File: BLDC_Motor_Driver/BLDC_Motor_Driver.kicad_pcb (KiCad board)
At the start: 4 copper layers, 95 x 95 mm, 139 parts, among them J101 Conn_01x08, J102 395221002, J103 USB4105-GF-A, J104 Conn_01x05, J105 Conn_01x05, J106 Conn_01x04, J107 395221005, J108 395221003, J109 Conn_02x12_Counter_Clockwise, J110 395221005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

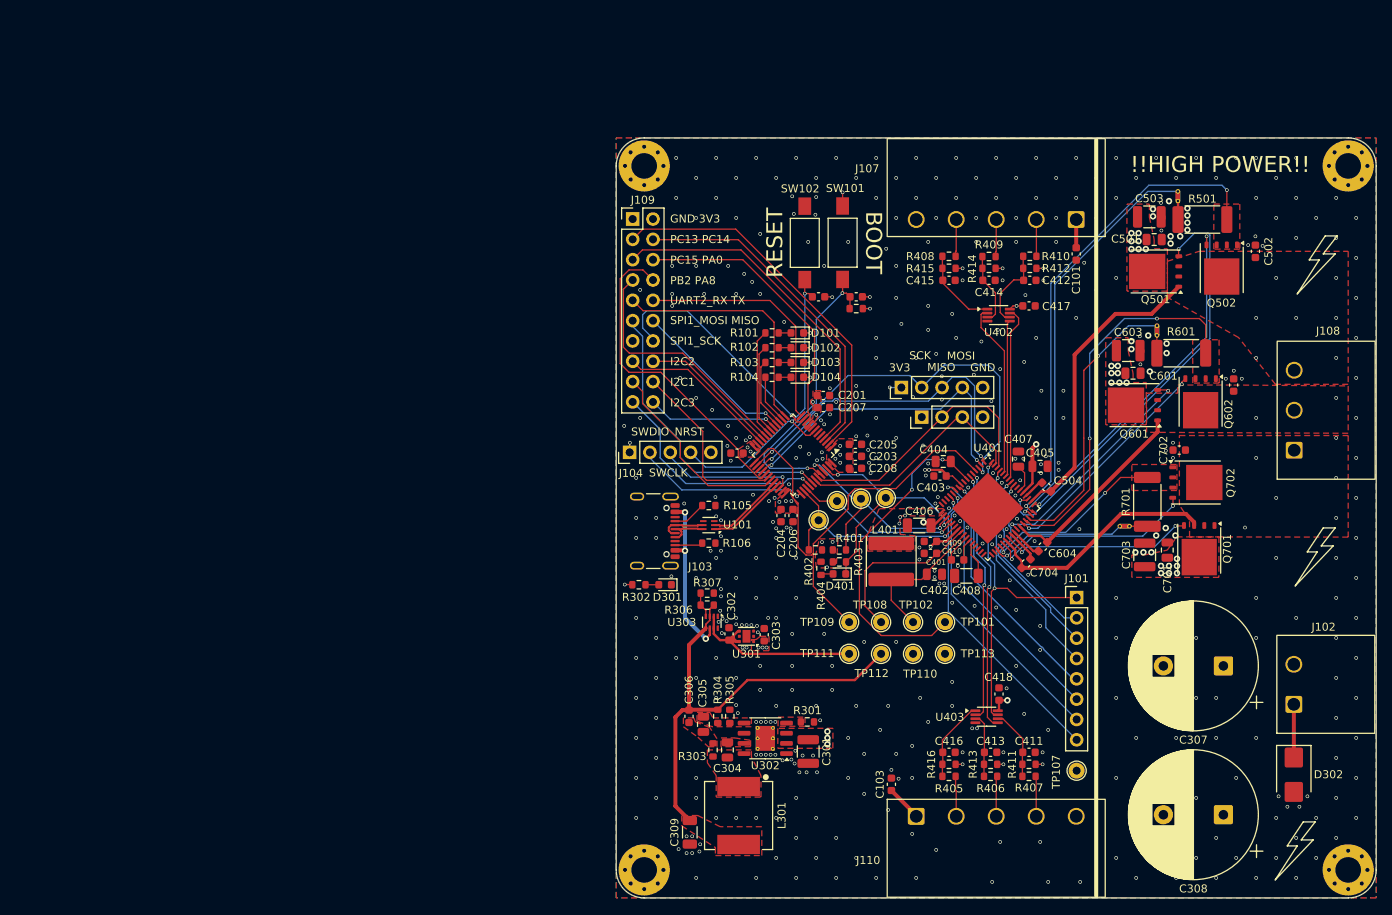
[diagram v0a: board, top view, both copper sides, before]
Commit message: silkscreen improvements and minor cleanup
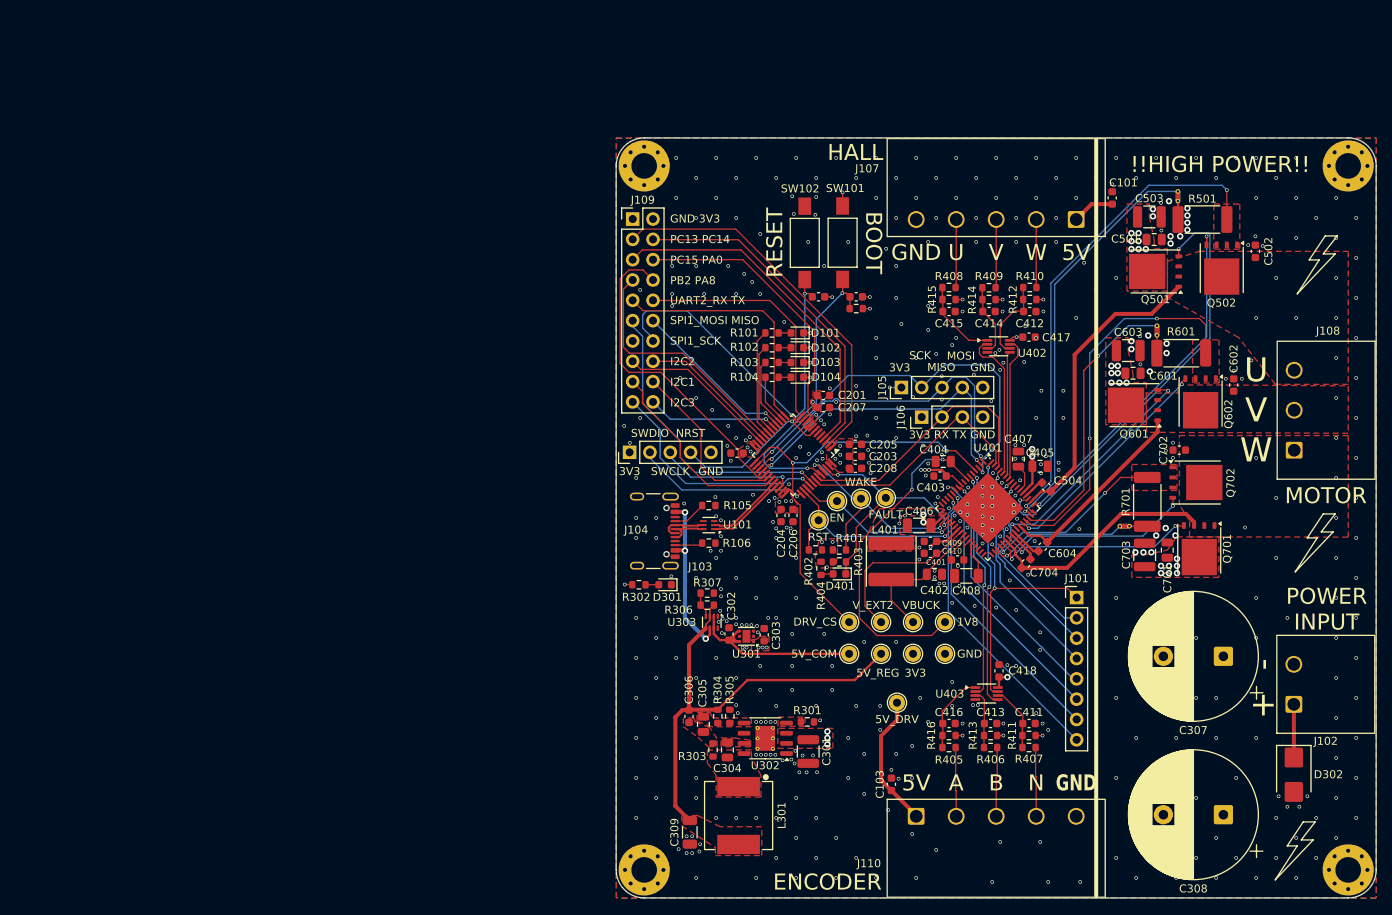
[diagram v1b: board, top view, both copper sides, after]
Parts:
- moved TP107 24.0 mm to (210.1, 135.6)
- moved C101 8.32 mm to (237.0, 72.5), turned to 90 degrees
- moved C412 3.90 mm to (226.7, 86.7)
- moved C414 3.90 mm to (221.6, 86.7)
- moved C415 3.90 mm to (216.6, 86.7)
- moved R408 3.90 mm to (216.6, 83.7)
- moved R409 3.90 mm to (221.6, 83.7)
- moved R412 3.90 mm to (226.7, 85.2)
- moved R414 3.90 mm to (221.6, 85.2)
- moved R415 3.90 mm to (216.6, 85.2)
- moved C417 3.90 mm to (226.6, 89.9)
- moved R410 3.90 mm to (226.7, 83.7)
- moved U402 3.90 mm to (222.8, 91.0)
- moved C411 3.60 mm to (226.6, 138.2)
- moved C413 3.60 mm to (221.8, 138.2)
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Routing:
- net +36V: track 89.3 -> 61.8 mm, vias 26 -> 28
- net /5V_DRV: track 60.0 -> 74.1 mm
- net /HALL_W_CONN: track 5.10 -> 9.53 mm
- net /HALL_V_CONN: track 4.66 -> 8.56 mm
- net /HALL_U_CONN: track 4.63 -> 8.53 mm
- net /Gate-Driver/HALL_V: track 19.6 -> 15.7 mm
- net /ENC_A_CONN: track 4.97 -> 8.63 mm
- net /ENC_N_CONN: track 5.03 -> 8.63 mm
- net /ENC_B_CONN: track 5.05 -> 8.65 mm
- net /Gate-Driver/HALL_U: track 22.0 -> 18.4 mm
- net /DRIVER_CS: track 57.9 -> 54.6 mm, vias 0 -> 2
- net /Gate-Driver/HALL_W: track 22.0 -> 19.0 mm
- net /Gate-Driver/ENC_B: track 33.2 -> 30.3 mm
- net /Gate-Driver/ENC_N: track 31.5 -> 28.7 mm
- net /Gate-Driver/ENC_A/TXEN: track 43.6 -> 40.9 mm
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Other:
- board text added: "+"
- board text added: "-"
- board text added: "3V3 RX TX GND"
- board text added: "5V"
- board text added: "5V_COM"
- board text added: "A"
- board text added: "B"
- board text added: "DRV_CS"
- board text added: "EN"
- board text added: "ENCODER"
- board text added: "HALL"
- board text added: "MOTOR"
- board text added: "N"
- board text added: "POWER INPUT"
- board text added: "U"
- board text added: "V"
- board text added: "W"
- board text removed: "5V_COMM"
- board text removed: "TP101"
- board text removed: "TP102"
- board text removed: "TP107"
- board text removed: "TP108"
- board text removed: "TP109"
- board text removed: "TP110"
- board text removed: "TP111"
- board text removed: "TP112"
- board text removed: "TP113"

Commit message: more final tweaks
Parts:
- moved D101 76.5 mm to (122.6, 74.4)
- moved D102 76.5 mm to (122.6, 76.2)
- moved D104 76.5 mm to (122.6, 79.9)
- moved L301 76.5 mm to (115.3, 134.7)
- moved R302 76.5 mm to (102.8, 105.9)
- moved SW102 76.5 mm to (123.6, 63.1)
- moved TP105 76.5 mm to (125.3, 97.8)
- moved C101 76.5 mm to (162.0, 57.5)
- moved C102 76.5 mm to (130.0, 69.9)
- moved C103 76.5 mm to (134.4, 130.8)
- moved C104 76.5 mm to (125.3, 69.9)
- moved C201 76.5 mm to (125.9, 83.7)
- moved C202 76.5 mm to (115.1, 89.4)
- moved C203 76.5 mm to (129.9, 89.8)
- moved C204 76.5 mm to (120.6, 97.2)
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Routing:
- net +3V3: track 12.2 -> 11.0 mm, vias 25 -> 24
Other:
- board text added: "Driver GPIO"
- board text added: "TXEN"
- board text removed: "ENC_A / TXEN"
